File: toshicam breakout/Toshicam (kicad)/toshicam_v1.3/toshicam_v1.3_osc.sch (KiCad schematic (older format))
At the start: 14 parts, among them P1 CONN_9, P2 CONN_9, U1 TLV0025, U2 TLV0015, U3 OSCILLATOR

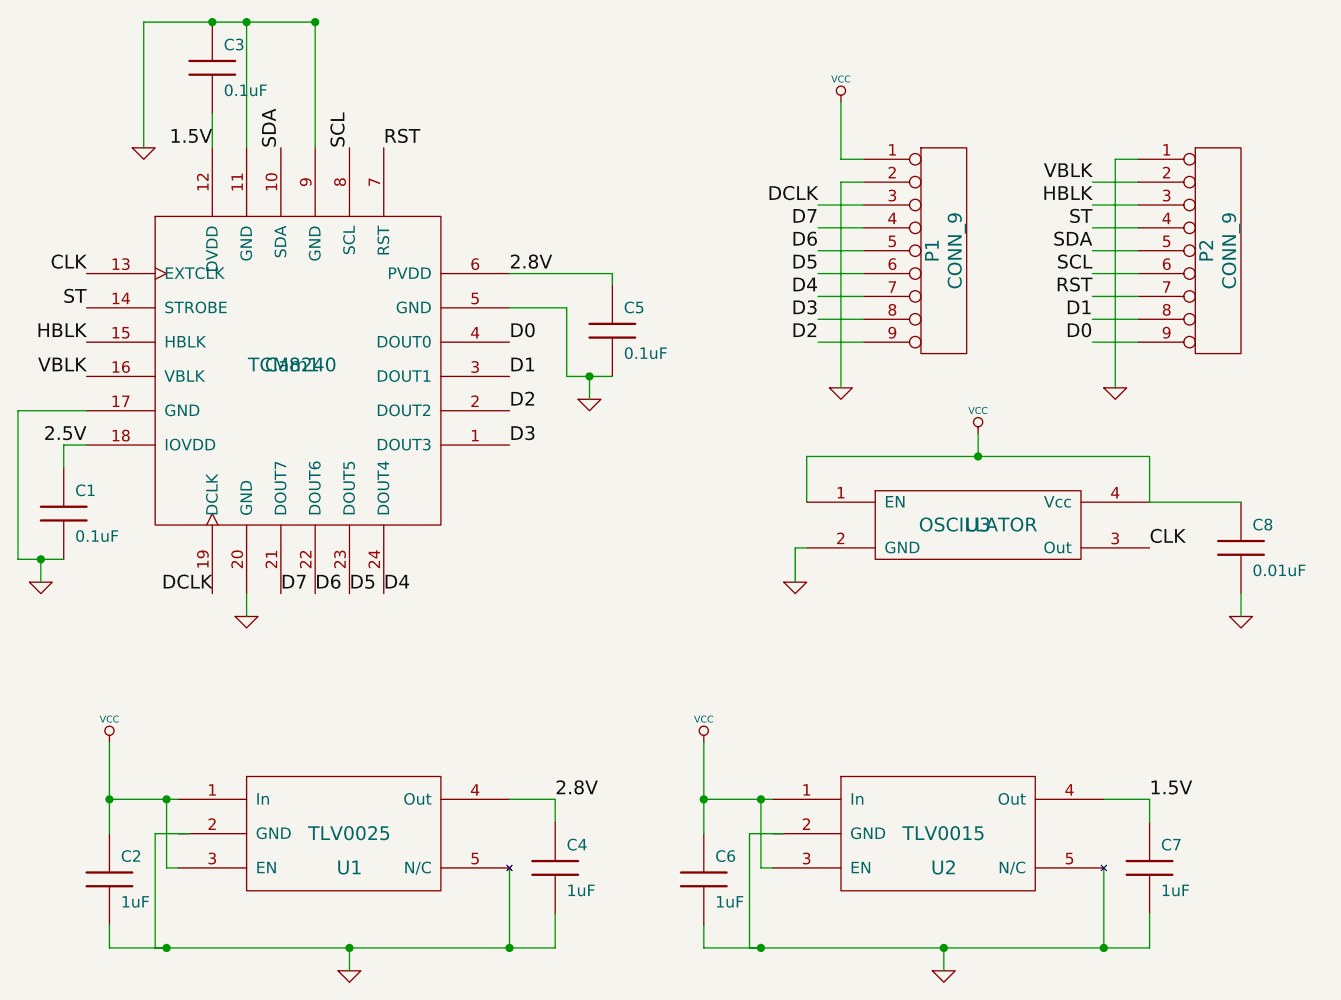
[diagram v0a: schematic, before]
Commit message: Uniformizacion de la denominacion de archivos y cambios menores en el esquemático
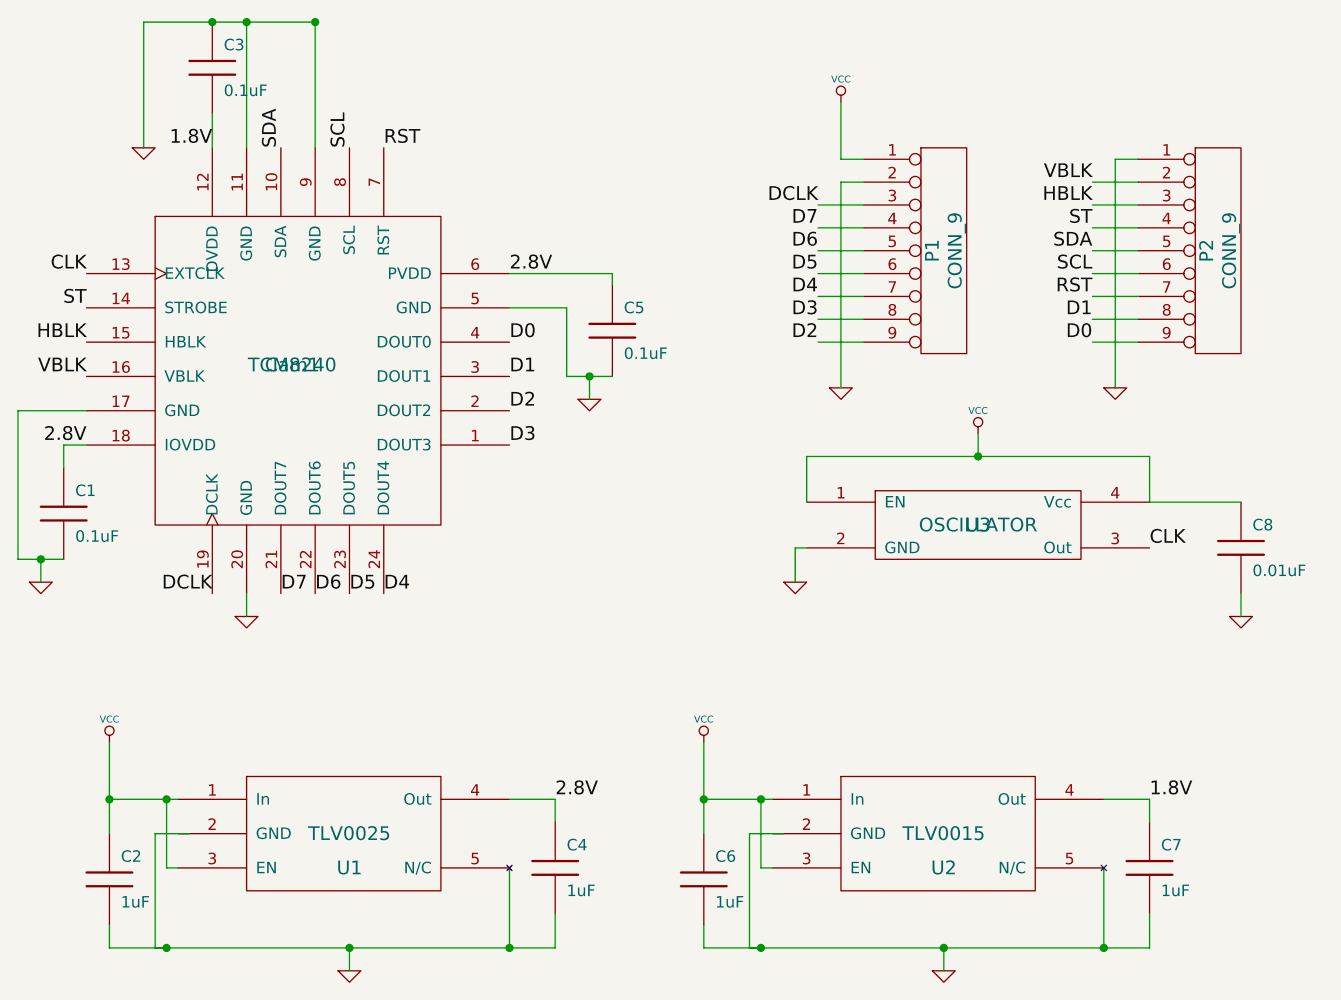
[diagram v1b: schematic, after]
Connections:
- net 2.5V is gone; now on net 2.8V: C1.1, Cam1.18 (IOVDD)
- net 1.5V renamed 1.8V
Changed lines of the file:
@@
-EESchema Schematic File Version 2  date Thu 12 May 2011 17:57:21 ART
-LIBS:power
-LIBS:device
-LIBS:transistors
-LIBS:conn
-LIBS:linear
-LIBS:regul
-LIBS:74xx
-LIBS:cmos4000
-LIBS:adc-dac
-LIBS:memory
-LIBS:xilinx
-LIBS:special
-LIBS:microcontrollers
-LIBS:dsp
-LIBS:microchip
-LIBS:analog_switches
-LIBS:motorola
-LIBS:texas
-LIBS:intel
-LIBS:audio
-LIBS:interface
-LIBS:digital-audio
-LIBS:philips
-LIBS:display
-LIBS:cypress
-LIBS:siliconi
-LIBS:opto
-LIBS:atmel
-LIBS:contrib
-LIBS:valves
-LIBS:oscillator
-LIBS:tcm8240
-LIBS:tlv0025
-EELAYER 25  0
+EESchema Schematic File Version 2  date Thu 12 May 2011 18:58:36 ART
+LIBS:power,/home/shokman/Documentos/Electronica/Club de robotica/Webcam pry/camarainalambrica/toshicam breakout/Toshicam (kicad)/toshicam_v1.3/library/tlv0025,/home/shokman/Documentos/Electronica/Club de robotica/Webcam pry/camarainalambrica/toshicam breakout/Toshicam (kicad)/toshicam_v1.3/library/tcm8240,/home/shokman/Documentos/Electronica/Club de robotica/Webcam pry/camarainalambrica/toshicam breakout/Toshicam (kicad)/toshicam_v1.3/library/oscillator,device,transistors,conn,linear,regul,74xx,cmos4000,adc-dac,memory,xilinx,special,microcontrollers,dsp,microchip,analog_switches,motorola,texas,intel,audio,interface,digital-audio,philips,display,cypress,siliconi,opto,atmel,contrib,valves
+EELAYER 24  0
 EELAYER END
 $Descr A4 11700 8267
@@
 $EndComp
 Text Label 6500 4800 0    60   ~ 0
-1.5V
+1.8V
 $Comp
 L VCC #PWR05
@@
 RST
 Text Label 2400 1950 2    60   ~ 0
-1.5V
+1.8V
 Text Label 3700 2500 0    60   ~ 0
 2.8V
 Text Label 1850 3250 2    60   ~ 0
-2.5V
+2.8V
 Text Label 1850 2500 2    60   ~ 0
 CLK

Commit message: Se realizaron los cambios: - La tensión mal llamada 1.8V fue corregida a 1.5V en el .sch y .brd - Se volvió a un ancho de 1"!!! Compatible con el breakout de SPARKFUN con capacitores 1206
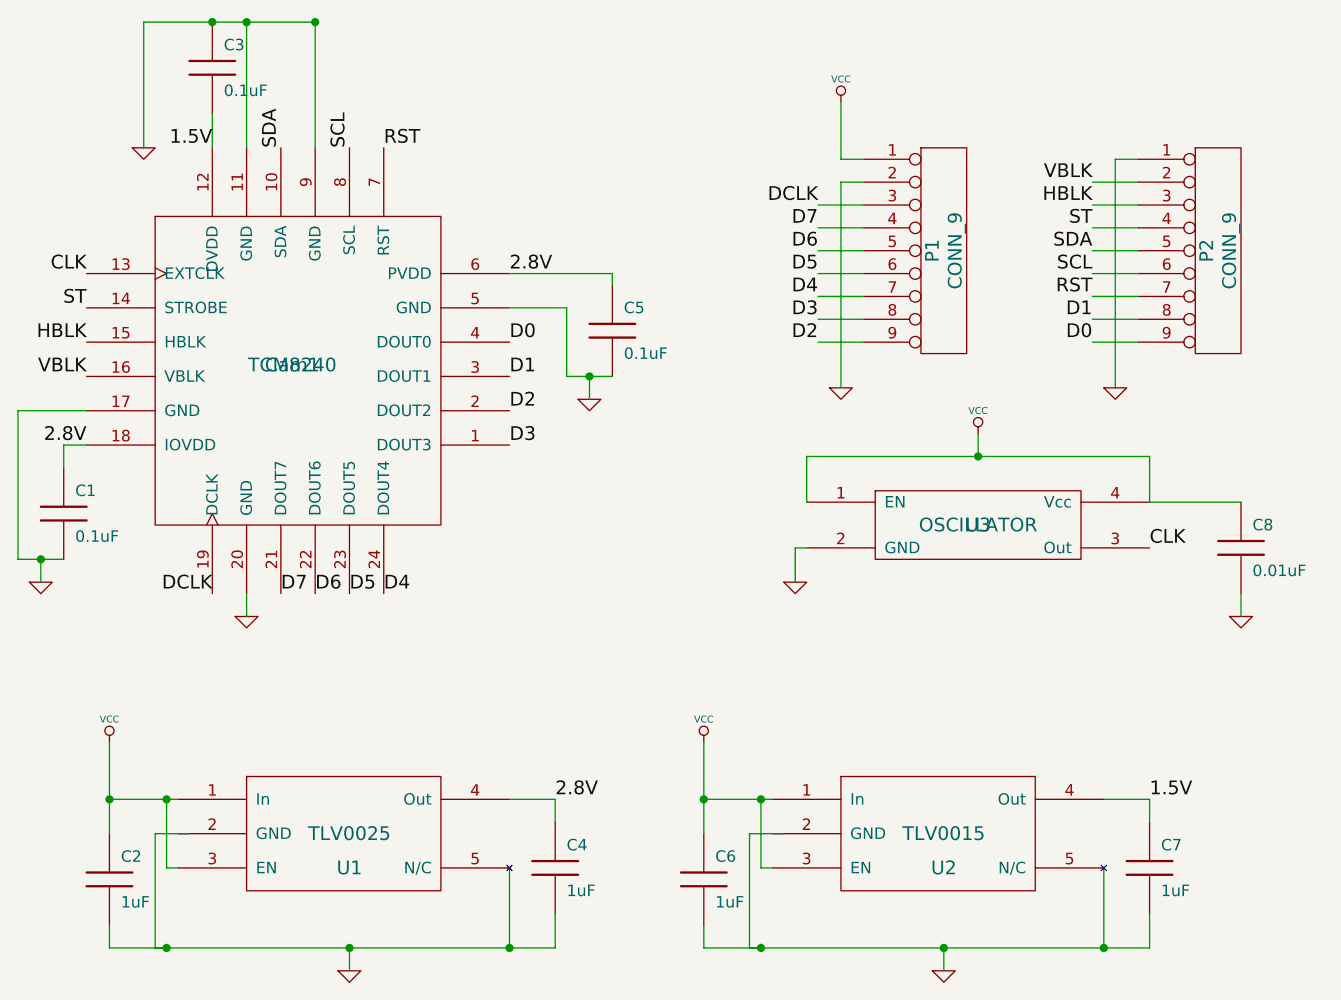
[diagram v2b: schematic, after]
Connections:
- net 1.8V renamed 1.5V
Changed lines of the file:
@@
-EESchema Schematic File Version 2  date Thu 12 May 2011 18:58:36 ART
-LIBS:power,/home/shokman/Documentos/Electronica/Club de robotica/Webcam pry/camarainalambrica/toshicam breakout/Toshicam (kicad)/toshicam_v1.3/library/tlv0025,/home/shokman/Documentos/Electronica/Club de robotica/Webcam pry/camarainalambrica/toshicam breakout/Toshicam (kicad)/toshicam_v1.3/library/tcm8240,/home/shokman/Documentos/Electronica/Club de robotica/Webcam pry/camarainalambrica/toshicam breakout/Toshicam (kicad)/toshicam_v1.3/library/oscillator,device,transistors,conn,linear,regul,74xx,cmos4000,adc-dac,memory,xilinx,special,microcontrollers,dsp,microchip,analog_switches,motorola,texas,intel,audio,interface,digital-audio,philips,display,cypress,siliconi,opto,atmel,contrib,valves
+EESchema Schematic File Version 2  date Sat 28 May 2011 16:22:21 ART
+LIBS:power
+LIBS:device
+LIBS:transistors
+LIBS:conn
+LIBS:linear
+LIBS:regul
+LIBS:74xx
+LIBS:cmos4000
+LIBS:adc-dac
+LIBS:memory
+LIBS:xilinx
+LIBS:special
+LIBS:microcontrollers
+LIBS:dsp
+LIBS:microchip
+LIBS:analog_switches
+LIBS:motorola
+LIBS:texas
+LIBS:intel
+LIBS:audio
+LIBS:interface
+LIBS:digital-audio
+LIBS:philips
+LIBS:display
+LIBS:cypress
+LIBS:siliconi
+LIBS:opto
+LIBS:atmel
+LIBS:contrib
+LIBS:valves
+LIBS:toshicam_v1.3_osc-cache
 EELAYER 24  0
 EELAYER END
@@
 Sheet 1 1
 Title ""
-Date "12 may 2011"
+Date "28 may 2011"
 Rev ""
 Comp ""
@@
 $EndComp
 Text Label 6500 4800 0    60   ~ 0
-1.8V
+1.5V
 $Comp
 L VCC #PWR05
@@
 RST
 Text Label 2400 1950 2    60   ~ 0
-1.8V
+1.5V
 Text Label 3700 2500 0    60   ~ 0
 2.8V
